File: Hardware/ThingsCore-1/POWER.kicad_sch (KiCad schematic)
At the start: 68 parts, among them Q1 Si2371EDS, Q2 Si2371EDS, Q3 2N7002, U3 TLV62569DBV, U4 TLV62569DBV, U5 TLV62569DBV, U7 STM32MP133DAE7

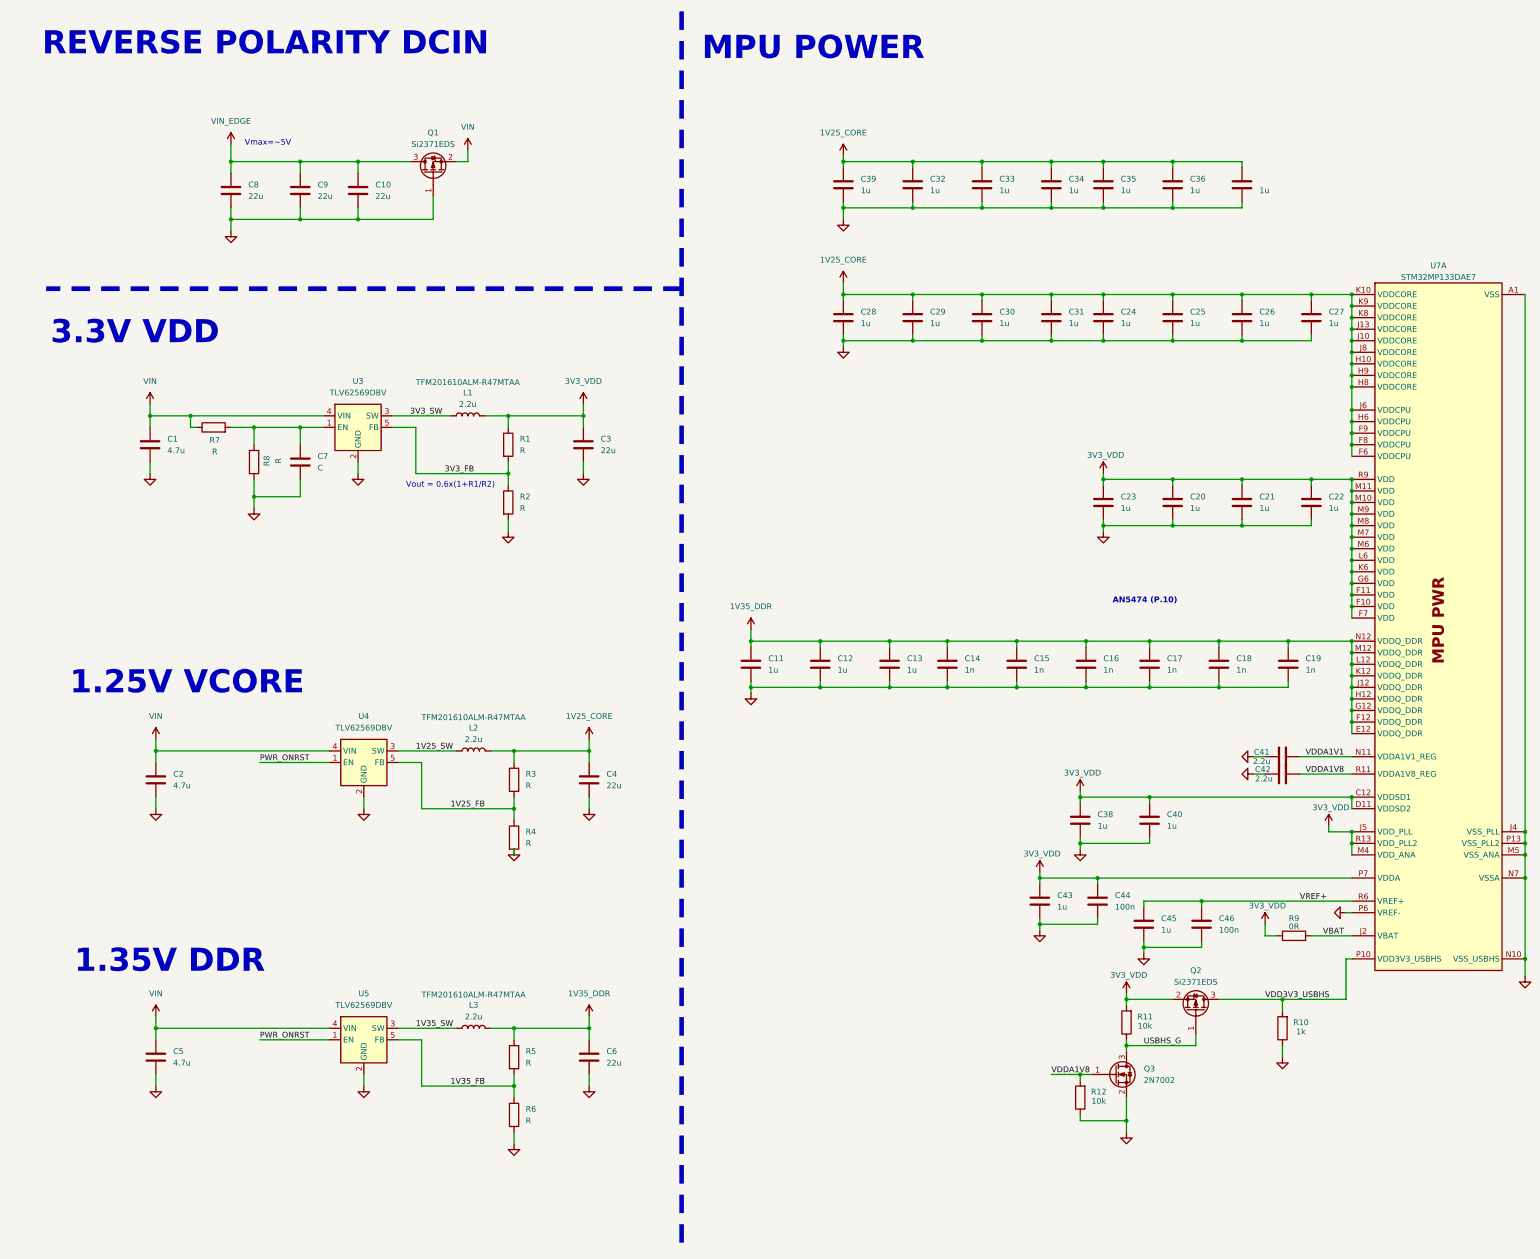
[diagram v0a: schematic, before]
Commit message: layout transciever components, pin selection and last components
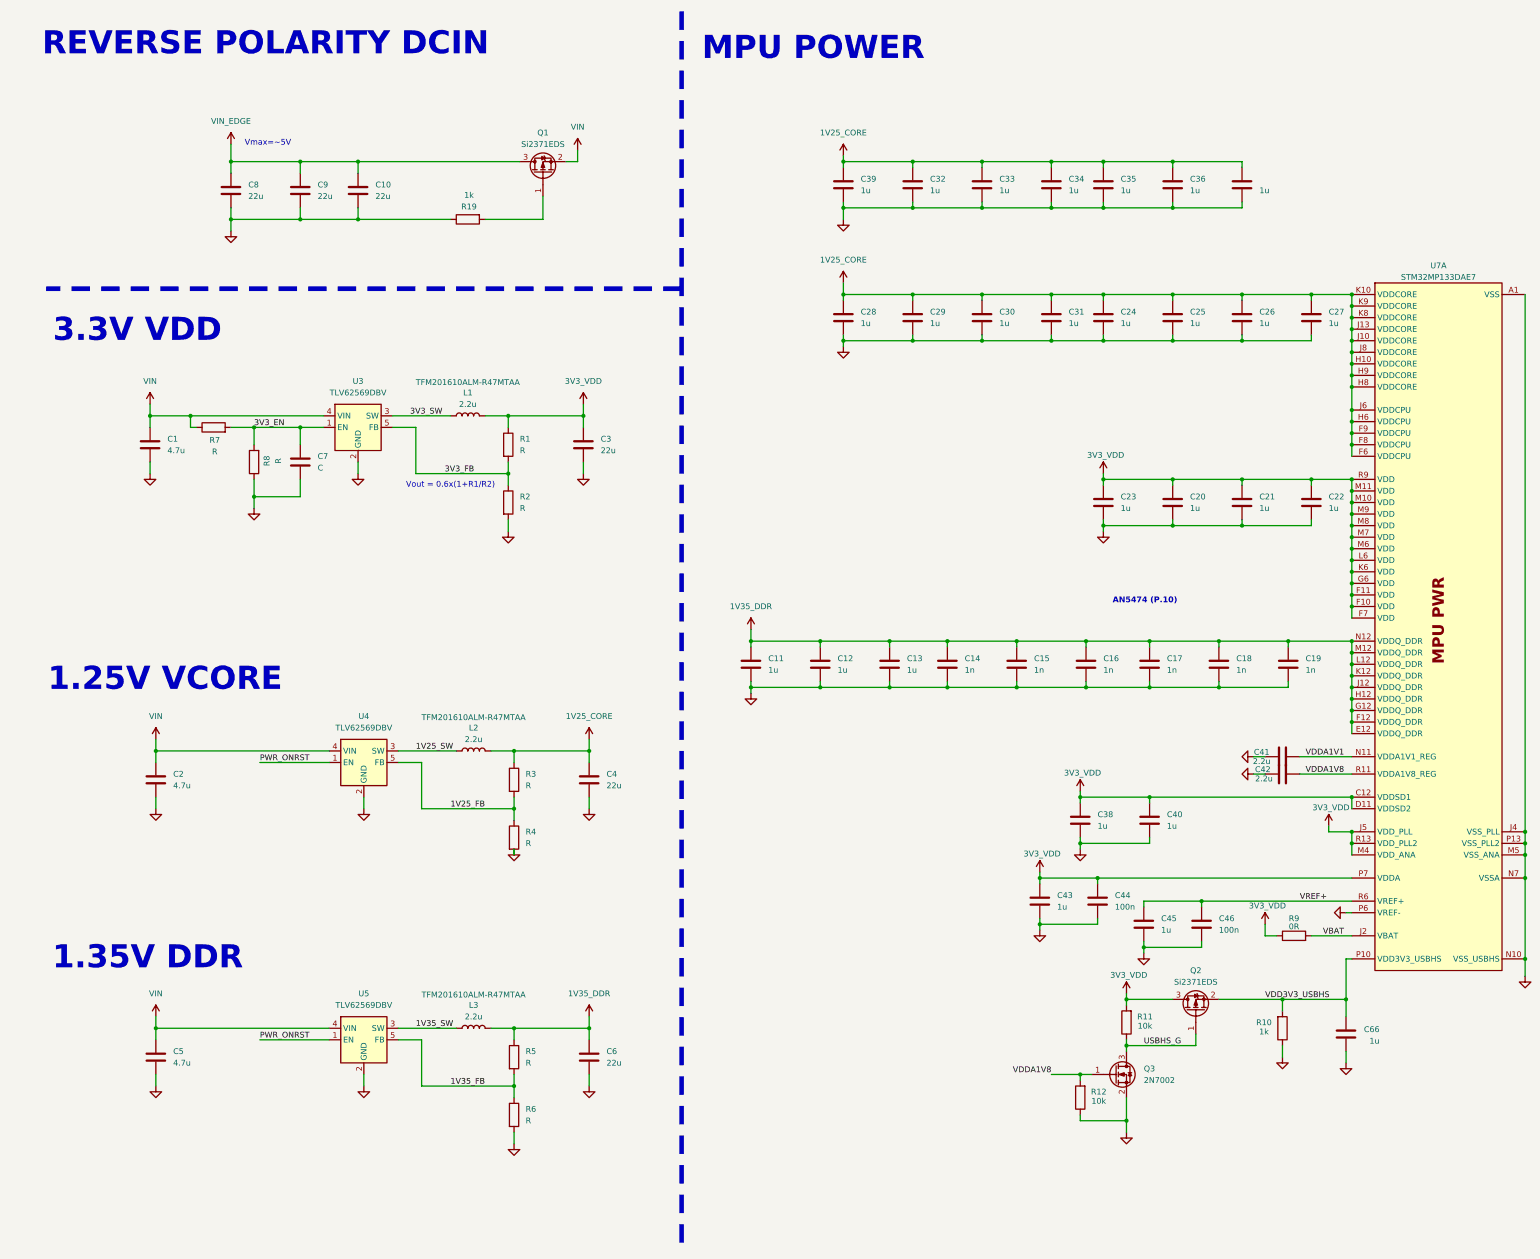
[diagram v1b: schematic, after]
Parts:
- added C66: 1u, Capacitor_SMD:C_0402_1005Metric, symbol Device:C
- added R19: 1k, Resistor_SMD:R_0402_1005Metric, symbol Device:R
- L1, L2, L3: footprint Inductor_SMD:L_Murata_DFE201610P -> ThingsCore-1:L_0805_2016
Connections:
- net 3V3_VDD: now also Q2.3 (D); no longer Q2.2 (S)
- net GND: now also C66.1, R19.1; no longer Q1.1 (G)
- net VDD3V3_USBHS: now also Q2.2 (S), C66.2; no longer Q2.3 (D)
- net 3V3_EN: now reaches C7.2, R7.2, R8.2, U3.1 (EN)
- new net: Q1.1 (G), R19.2
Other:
- moved on the sheet: Q1, Q2, R10

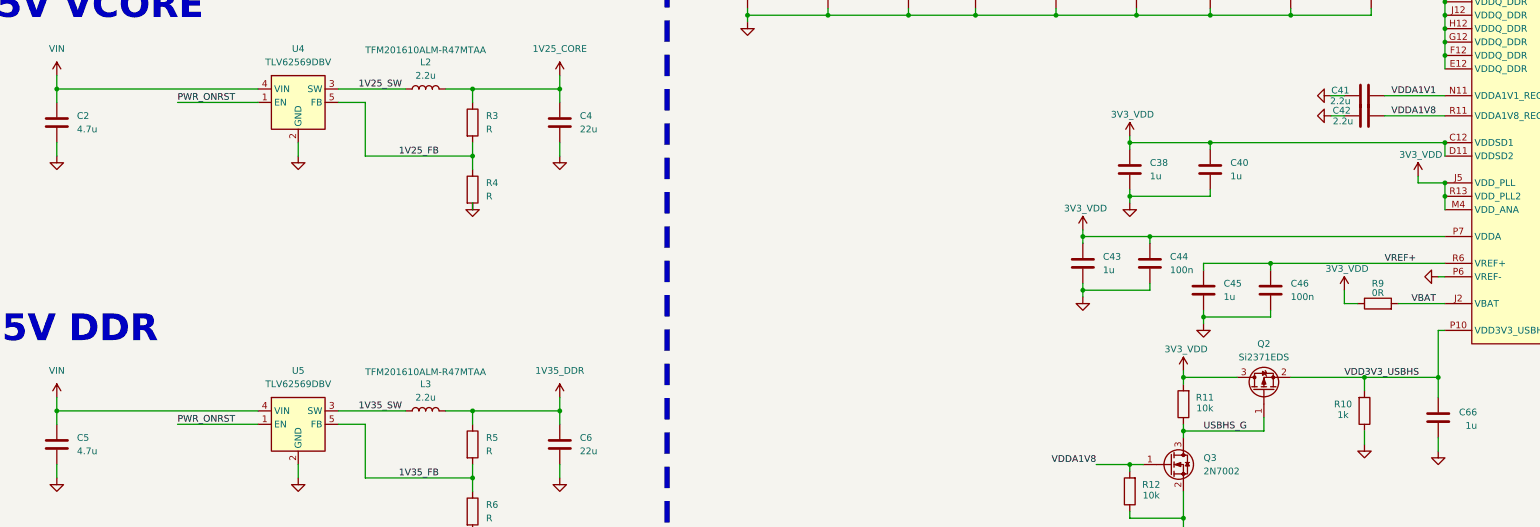
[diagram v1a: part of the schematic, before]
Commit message: pin assignment, rst,led, button pins left and checks
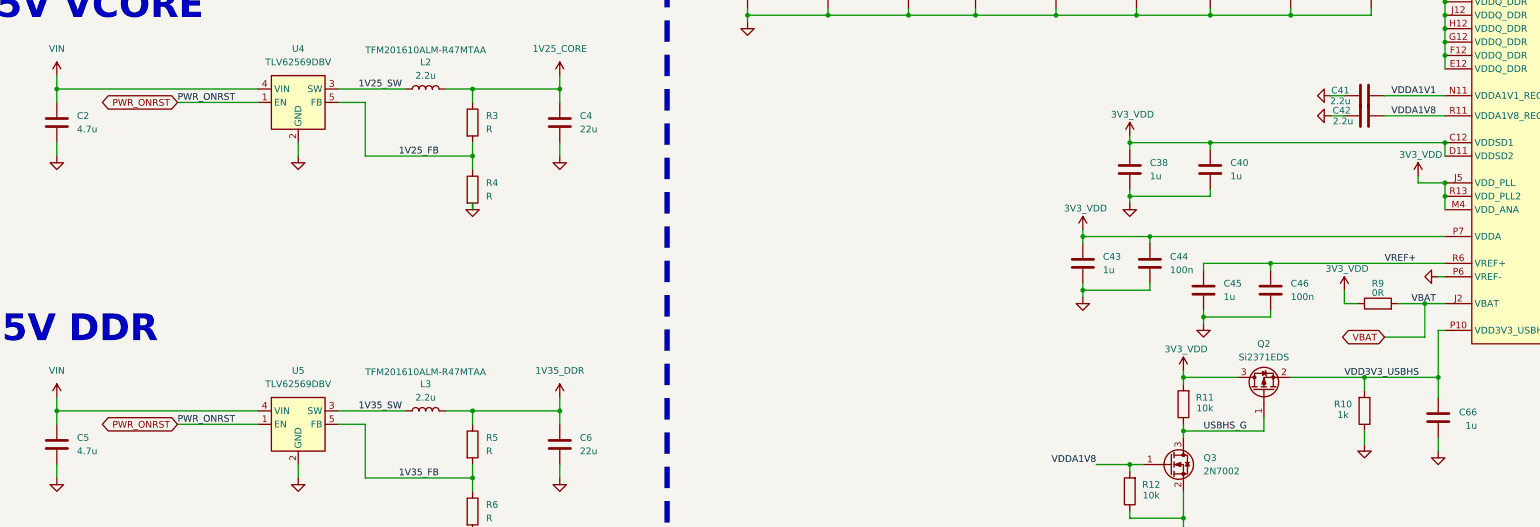
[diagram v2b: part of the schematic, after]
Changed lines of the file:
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@@
 	)
 	(junction
+		(at 295.91 215.9)
+		(diameter 0)
+		(color 0 0 0 0)
+	)
+	(junction
 		(at 337.82 203.2)
 		(diameter 0)
@@
 	(wire
 		(pts
-			(xy 299.72 215.9) (xy 290.83 215.9)
+			(xy 299.72 215.9) (xy 295.91 215.9)
 		)
 		(stroke
@@
 	(wire
 		(pts
+			(xy 288.29 222.25) (xy 295.91 222.25)
+		)
+		(stroke
+			(width 0)
+			(type default)
+		)
+	)
+	(wire
+		(pts
 			(xy 250.19 238.76) (xy 250.19 240.03)
 		)
@@
 	(wire
 		(pts
+			(xy 295.91 222.25) (xy 295.91 215.9)
+		)
+		(stroke
+			(width 0)
+			(type default)
+		)
+	)
+	(wire
+		(pts
 			(xy 167.64 148.59) (xy 167.64 151.13)
 		)
@@
 	(wire
 		(pts
+			(xy 295.91 215.9) (xy 290.83 215.9)
+		)
+		(stroke
+			(width 0)
+			(type default)
+		)
+	)
+	(wire
+		(pts
 			(xy 218.44 85.09) (xy 218.44 83.82)
 		)
@@
 		)
 	)
+	(global_label "VBAT"
+		(shape bidirectional)
+		(at 288.29 222.25 180)
+		(fields_autoplaced yes)
+		(effects
+			(font
+				(size 1.27 1.27)
+			)
+			(justify right)
+		)
+		(property "Intersheetrefs" "${INTERSHEET_REFS}"
+			(at 279.7787 222.25 0)
+			(effects
+				(font
+					(size 1.27 1.27)
+				)
+				(justify right)
+				(hide yes)
+			)
+		)
+	)
+	(global_label "PWR_ONRST"
+		(shape bidirectional)
+		(at 59.69 238.76 180)
+		(fields_autoplaced yes)
+		(effects
+			(font
+				(size 1.27 1.27)
+			)
+			(justify right)
+		)
+		(property "Intersheetrefs" "${INTERSHEET_REFS}"
+			(at 44.5264 238.76 0)
+			(effects
+				(font
+					(size 1.27 1.27)
+				)
+				(justify right)
+				(hide yes)
+			)
+		)
+	)
+	(global_label "PWR_ONRST"
+		(shape bidirectional)
+		(at 59.69 177.8 180)
+		(fields_autoplaced yes)
+		(effects
+			(font
+				(size 1.27 1.27)
+			)
+			(justify right)
+		)
+		(property "Intersheetrefs" "${INTERSHEET_REFS}"
+			(at 44.5264 177.8 0)
+			(effects
+				(font
+					(size 1.27 1.27)
+				)
+				(justify right)
+				(hide yes)
+			)
+		)
+	)
